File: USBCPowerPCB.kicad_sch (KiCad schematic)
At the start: 31 parts, among them J1 UJ31-CH-31N-SMT-TR, J2 CC, J3 12V_OUT, J4 5V_ISOOUT, J5 12V_OUT_PIN, J6 5V_ISOOUT_PIN, J7 5V_UNISOOUT_PIN, U1 TVS2200DRV

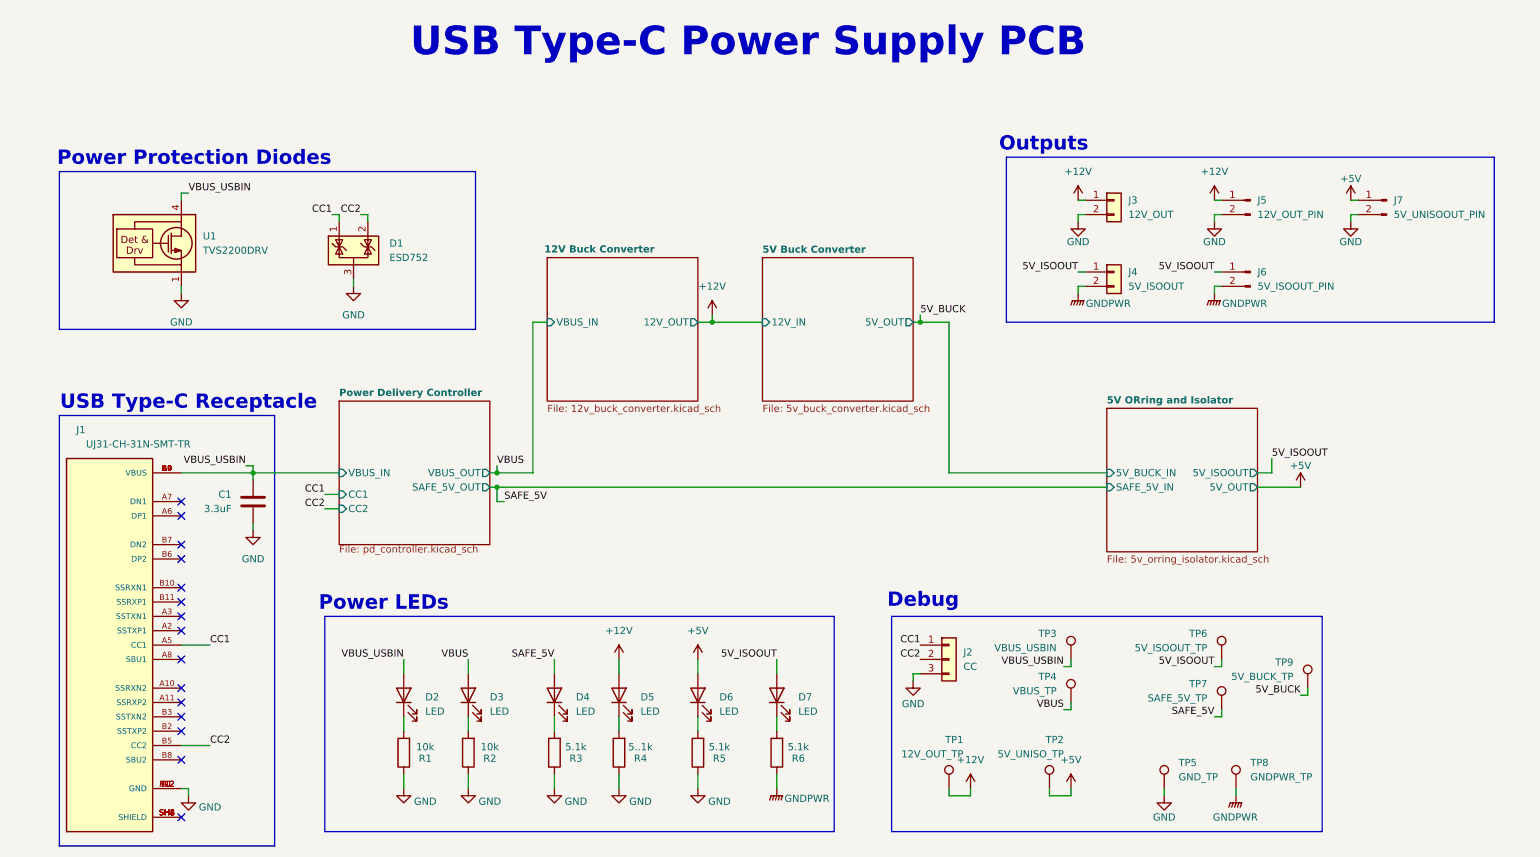
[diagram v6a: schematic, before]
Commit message: finished addressing review comments & organized bom with p/ns for everything
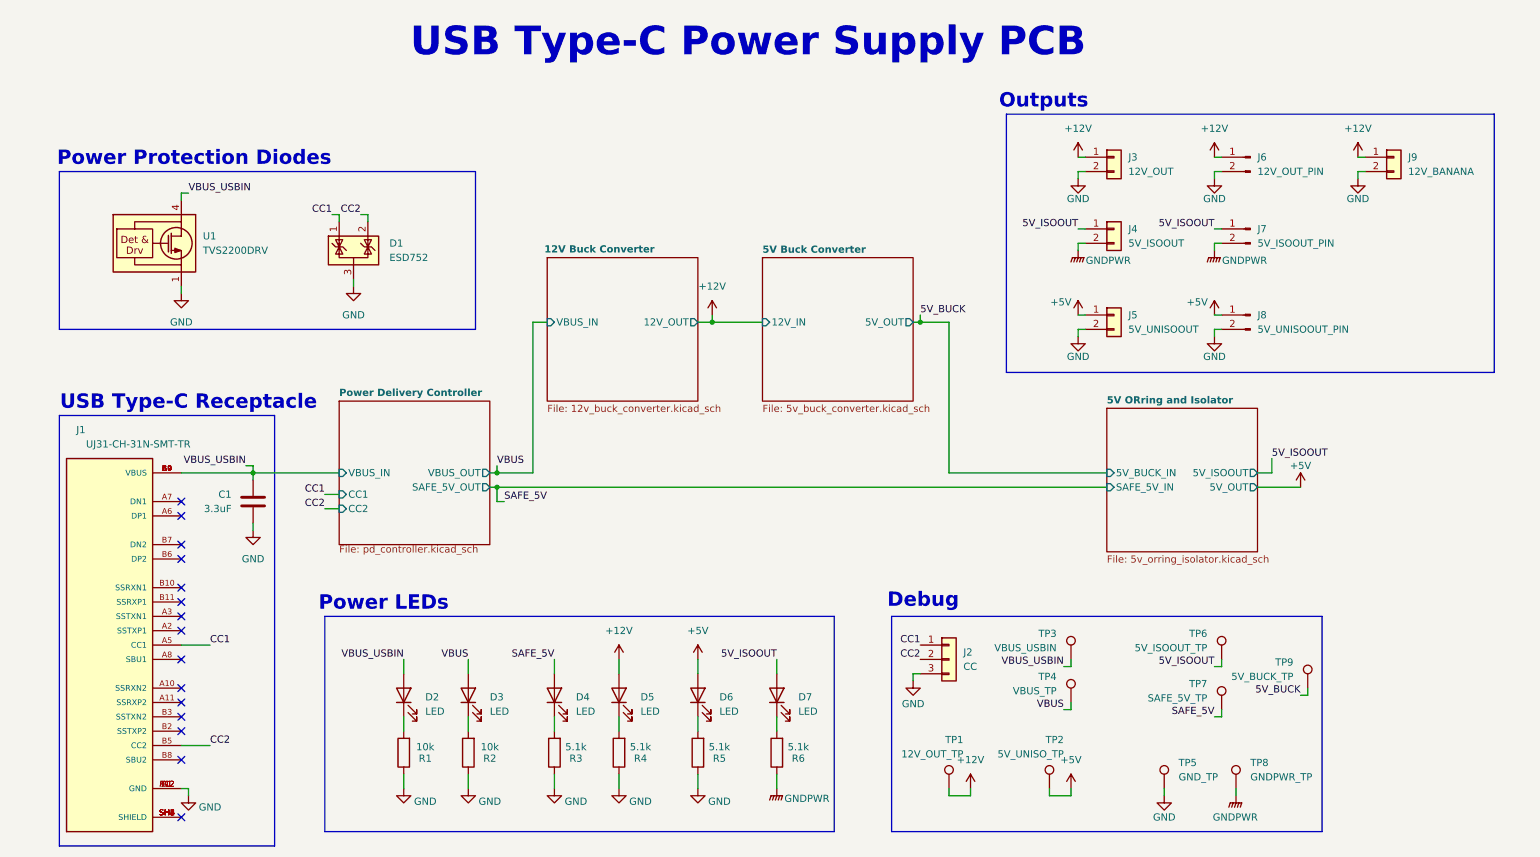
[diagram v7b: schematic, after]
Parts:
- added J5: 5V_UNISOOUT, UTSVT_Connectors:Molex_MicroFit3.0_1x2xP3.00mm_PolarizingPeg_Vertical, symbol Connector_Generic:Conn_01x02
- added J9: 12V_BANANA, Connector:Banana_Jack_2Pin, symbol Connector_Generic:Conn_01x02
- C1: Manufacturer_Name (none) -> TDK; Mouser Part Number (none) -> C2012X5R1H335K125AB; Vdc (none) -> 50V
- D1: Manufacturer_Name (none) -> Texas Instruments; Mouser Part Number (none) -> 595-ESD752DBZR
- D2, D3, D4, D5, D6, D7: Manufacturer_Name (none) -> Kingbright; Mouser Part Number APTD2012LCGCK -> 604-APTD2012LCGCK
- J1: MANUFACTURER CUI INC -> (none); MF CUI Devices -> (none); MP UJ31-CH-31N-SMT-TR -> (none); Manufacturer_Name (none) -> CUI Devices; Mouser Part Number (none) -> 490-UJ31-CH31NSMT-TR
- R1, R2: Manufacturer_Name (none) -> VISHAY; Mouser Part Number (none) -> CRCW080510K0FKEAC
- R3, R5, R6: Manufacturer_Name (none) -> VISHAY; Mouser Part Number (none) -> CRCW08055K10FKEAC
- R4: value 5..1k -> 5.1k; Manufacturer_Name (none) -> VISHAY; Mouser Part Number (none) -> CRCW08055K10FKEAC
- U1: Manufacturer_Name (none) -> Texas Instruments; Mouser Part Number (none) -> 595-TVS2200DRVR
- renumbered J5 to J6, J6 to J7, J7 to J8
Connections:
- net +12V: now also J9.1 (Pin_1)
- net +5V: now also J5.1 (Pin_1)
- net GND: now also J5.2 (Pin_2), J9.2 (Pin_2)
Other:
- moved on the sheet: J3, J4, J6, J7, J8

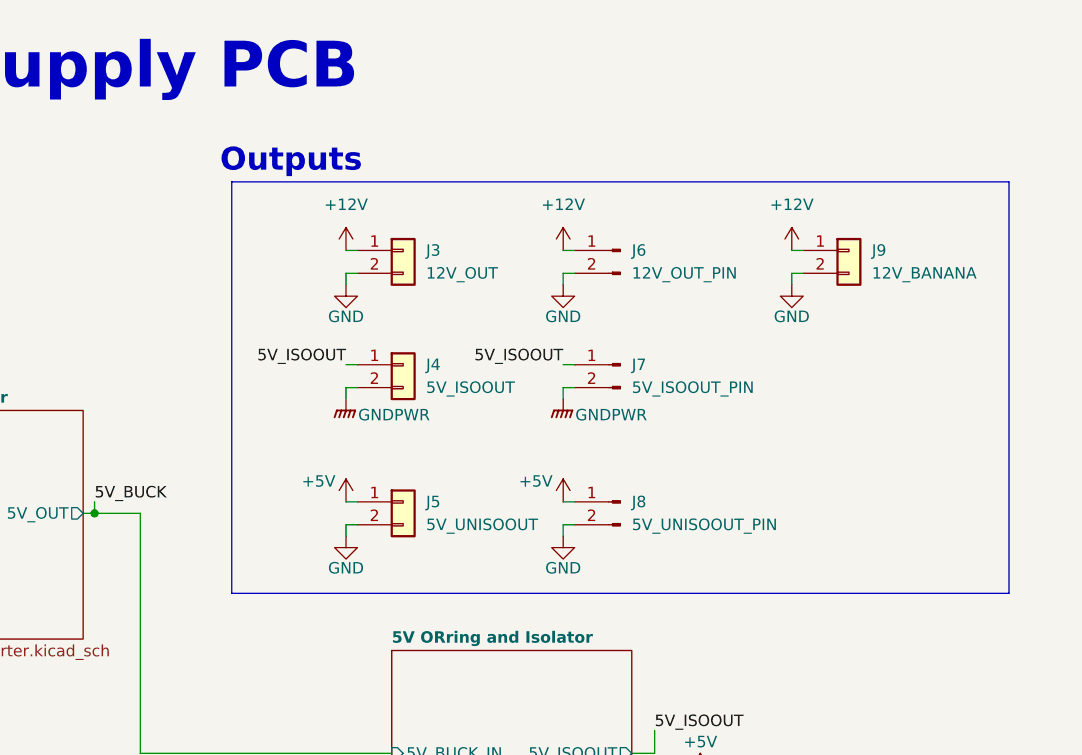
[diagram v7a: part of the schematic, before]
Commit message: added banana jacks for input/output to 12v buck, for isolated 12v buck testing. also filled in more part numbers for connectors.
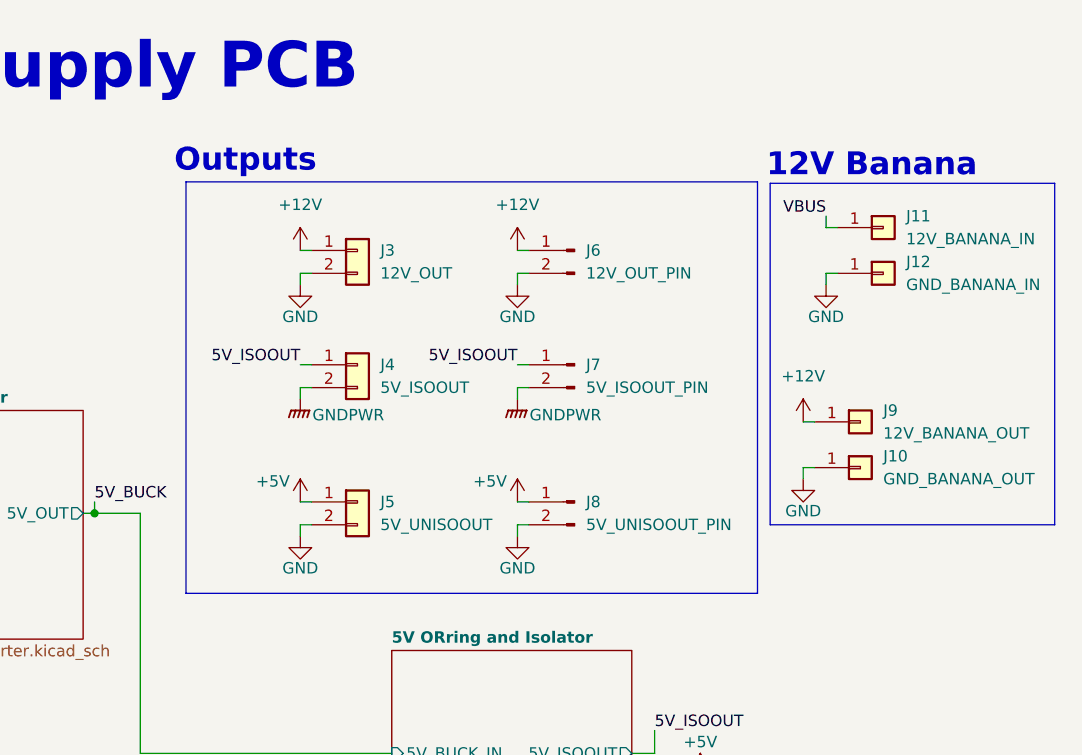
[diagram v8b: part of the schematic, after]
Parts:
- removed J9: 12V_BANANA, Connector:Banana_Jack_2Pin, symbol Connector_Generic:Conn_01x02
- added J10: GND_BANANA_OUT, UTSVT_Connectors:Banana_Jack_Horizontal, symbol Connector_Generic:Conn_01x01
- added J11: 12V_BANANA_IN, UTSVT_Connectors:Banana_Jack_Horizontal, symbol Connector_Generic:Conn_01x01
- added J12: GND_BANANA_IN, UTSVT_Connectors:Banana_Jack_Horizontal, symbol Connector_Generic:Conn_01x01
- added J9: 12V_BANANA_OUT, UTSVT_Connectors:Banana_Jack_Horizontal, symbol Connector_Generic:Conn_01x01
- J3, J4, J5: Manufacturer_Name (none) -> Molex; Mouser Part Number (none) -> 436500215
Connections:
- net +12V: now also J9.1 (Pin_1)
- net GND: now also J10.1 (Pin_1), J12.1 (Pin_1)
- net VBUS: now also J11.1 (Pin_1)
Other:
- note added: "12V Banana"
- moved on the sheet: J3, J4, J5, J6, J7, J8
